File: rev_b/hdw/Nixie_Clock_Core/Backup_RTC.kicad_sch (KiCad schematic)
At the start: 14 parts, among them U1201 DS3231MZ, U1202 TLV6700

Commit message: lots of rev B control board schematic progress
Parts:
- renumbered BT1202 to BT?, BT1201 to BT?, C1202 to C?, C1205 to C?, C1204 to C?, C1203 to C?, C1201 to C?, DOC1201 to DOC?, R1203 to R?, R1201 to R?, R1202 to R?, TP1201 to TP?, U1202 to U?, U1201 to U?

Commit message: more rev b sch progress
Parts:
- removed R?: 1.07M, Resistors_SMD:R_0402, symbol Custom_Library:R_Custom
- added R?: 1M, Resistors_SMD:R_0402, symbol Custom_Library:R_Custom
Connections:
- net VBAT: now also R?.1
- net VBAT_ADC: now also R?.2
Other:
- moved on the sheet: C?, R?, TP?

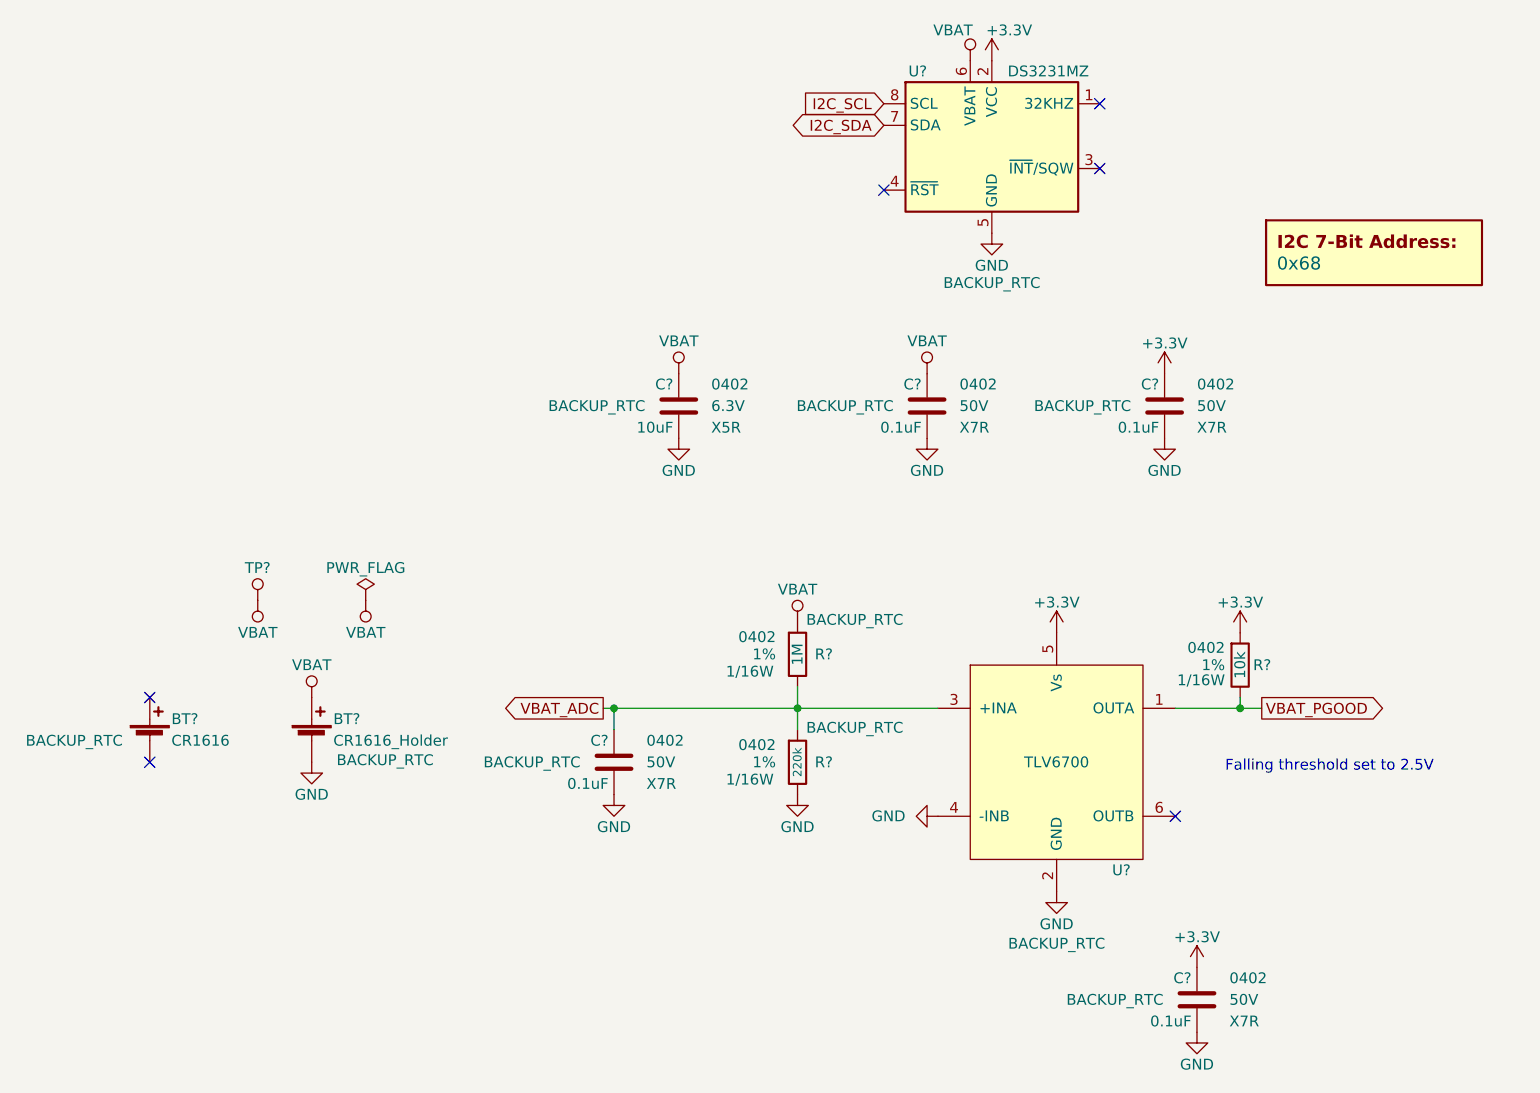
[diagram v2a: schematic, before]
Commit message: updated footprints, ran some DRC
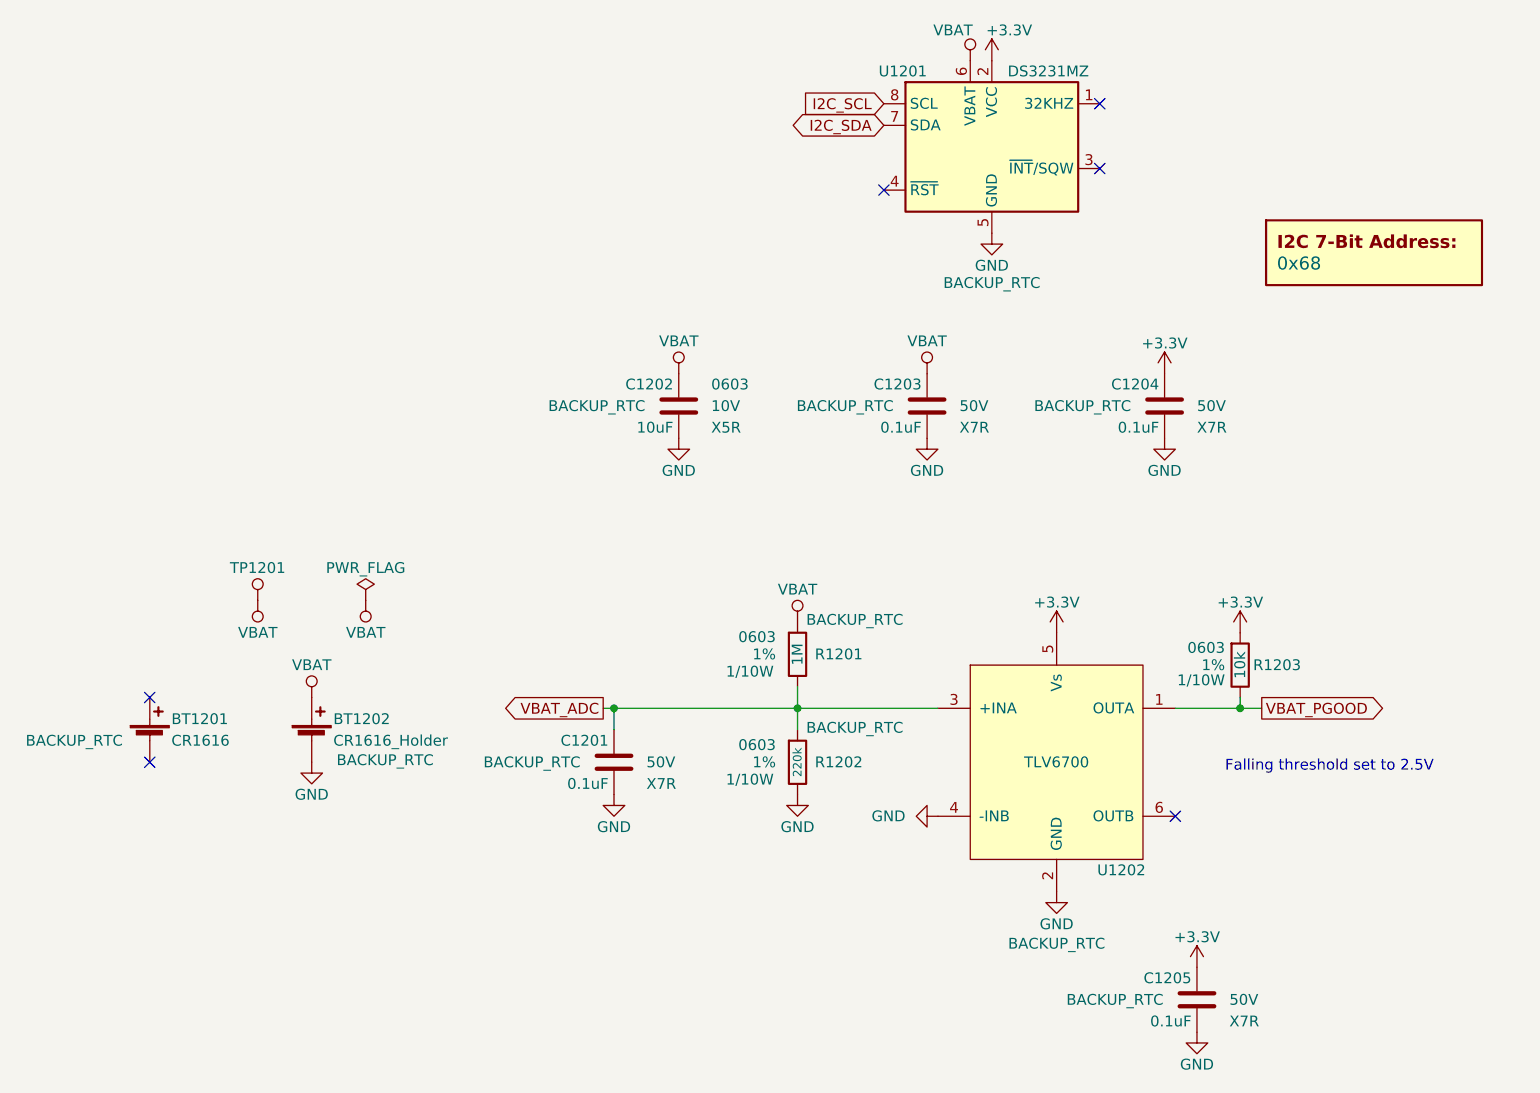
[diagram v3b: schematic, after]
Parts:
- C1201, C1203, C1204, C1205: renamed from C?; footprint Capacitors_SMD:C_0402 -> Capacitors_SMD:C_0603; Digi-Key PN 490-10698-1-ND -> (none); display_footprint 0402 -> (none)
- C1202: renamed from C?; footprint Capacitors_SMD:C_0402 -> Capacitors_SMD:C_0603; Digi-Key PN 1276-1451-1-ND -> (none); Voltage 6.3V -> 10V; display_footprint 0402 -> 0603
- R1201: renamed from R?; footprint Resistors_SMD:R_0402 -> Resistors_SMD:R_0603; Wattage 1/16W -> 1/10W; display_footprint 0402 -> 0603
- R1202: renamed from R?; footprint Resistors_SMD:R_0402 -> Resistors_SMD:R_0603; Digi-Key PN RMCF0402FT220KCT-ND -> (none); Wattage 1/16W -> 1/10W; display_footprint 0402 -> 0603
- R1203: renamed from R?; footprint Resistors_SMD:R_0402 -> Resistors_SMD:R_0603; Digi-Key PN RMCF0402FT10K0CT-ND -> (none); Wattage 1/16W -> 1/10W; display_footprint 0402 -> 0603
- gave numbers to parts that had none: 6

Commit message: hid all passive refdes on core PCB
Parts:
- C1201, C1203, C1204, C1205: Digi-Key PN (none) -> 1276-1935-1-ND; display_footprint (none) -> 0603
- C1202: Digi-Key PN (none) -> 1276-1871-1-ND
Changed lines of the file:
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@@
       (effects (font (size 1.27 1.27)))
     )
-    (property "Digi-Key PN" "" (at 123.19 77.47 0)
+    (property "Digi-Key PN" "1276-1871-1-ND" (at 123.19 77.47 0)
       (effects (font (size 1.27 1.27)) hide)
     )
@@
       (effects (font (size 1.27 1.27)) hide)
     )
-    (property "display_footprint" "" (at 187.96 144.78 0)
+    (property "display_footprint" "0603" (at 187.96 144.78 0)
       (effects (font (size 1.27 1.27)) (justify right))
     )
@@
       (effects (font (size 1.27 1.27)))
     )
-    (property "Digi-Key PN" "" (at 184.15 147.32 0)
+    (property "Digi-Key PN" "1276-1935-1-ND" (at 184.15 147.32 0)
       (effects (font (size 1.27 1.27)) hide)
     )
@@
       (effects (font (size 1.27 1.27)) hide)
     )
-    (property "display_footprint" "" (at 184.15 74.93 0)
+    (property "display_footprint" "0603" (at 184.15 74.93 0)
       (effects (font (size 1.27 1.27)) (justify right))
     )
@@
       (effects (font (size 1.27 1.27)))
     )
-    (property "Digi-Key PN" "" (at 180.34 77.47 0)
+    (property "Digi-Key PN" "1276-1935-1-ND" (at 180.34 77.47 0)
       (effects (font (size 1.27 1.27)) hide)
     )
@@
       (effects (font (size 1.27 1.27)) hide)
     )
-    (property "display_footprint" "" (at 156.21 74.93 0)
+    (property "display_footprint" "0603" (at 156.21 74.93 0)
       (effects (font (size 1.27 1.27)) (justify right))
     )
@@
       (effects (font (size 1.27 1.27)))
     )
-    (property "Digi-Key PN" "" (at 152.4 77.47 0)
+    (property "Digi-Key PN" "1276-1935-1-ND" (at 152.4 77.47 0)
       (effects (font (size 1.27 1.27)) hide)
     )
@@
       (effects (font (size 1.27 1.27)) hide)
     )
-    (property "display_footprint" "" (at 119.38 116.84 0)
+    (property "display_footprint" "0603" (at 119.38 116.84 0)
       (effects (font (size 1.27 1.27)) (justify right))
     )
@@
       (effects (font (size 1.27 1.27)))
     )
-    (property "Digi-Key PN" "" (at 115.57 119.38 0)
-      (effects (font (size 1.27 1.27)) hide)
-    )
+    (property "Digi-Key PN" "1276-1935-1-ND" (at 115.57 119.38 0)
+      (effects (font (size 1.27 1.27)) hide)
+    )

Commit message: added BOM
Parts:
- R1201: Digi-Key PN (none) -> 541-1.00MHCT-ND
- R1202: Digi-Key PN (none) -> 541-4039-1-ND
- R1203: Digi-Key PN (none) -> 541-10.0KHCT-ND
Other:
- title: (none) -> Nixie Clock Redux Core Board
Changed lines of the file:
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@@
   (paper "A")
   (title_block
-    (date "2023-05-12")
-    (rev "PRELIM")
+    (title "Nixie Clock Redux Core Board")
+    (date "2023-07-30")
+    (rev "B")
     (company "Drew Maatman")
   )
@@
     (effects (font (size 1.27 1.27)) (justify left bottom))
   )
-  (global_label "VBAT_ADC" (shape output) (at 114.3 113.03 180)
+  (global_label "VBAT_ADC" (shape output) (at 114.3 113.03 180) (fields_autoplaced)
     (effects (font (size 1.27 1.27)) (justify right))
-    (property "Intersheetrefs" "${INTERSHEET_REFS}" (at 114.3 113.03 0)
-      (effects (font (size 1.27 1.27)) hide)
-    )
-  )
-  (global_label "I2C_SDA" (shape bidirectional) (at 147.32 44.45 180)
+    (property "Intersheetrefs" "${INTERSHEET_REFS}" (at 102.3832 113.03 0)
+      (effects (font (size 1.27 1.27)) (justify right))
+    )
+  )
+  (global_label "I2C_SDA" (shape bidirectional) (at 147.32 44.45 180) (fields_autoplaced)
     (effects (font (size 1.27 1.27)) (justify right))
-    (property "Intersheetrefs" "${INTERSHEET_REFS}" (at 147.32 44.45 0)
-      (effects (font (size 1.27 1.27)) hide)
-    )
-  )
-  (global_label "I2C_SCL" (shape input) (at 147.32 41.91 180)
+    (property "Intersheetrefs" "${INTERSHEET_REFS}" (at 135.6829 44.45 0)
+      (effects (font (size 1.27 1.27)) (justify right))
+    )
+  )
+  (global_label "I2C_SCL" (shape input) (at 147.32 41.91 180) (fields_autoplaced)
     (effects (font (size 1.27 1.27)) (justify right))
-    (property "Intersheetrefs" "${INTERSHEET_REFS}" (at 147.32 41.91 0)
-      (effects (font (size 1.27 1.27)) hide)
-    )
-  )
-  (global_label "VBAT_PGOOD" (shape output) (at 191.77 113.03 0)
+    (property "Intersheetrefs" "${INTERSHEET_REFS}" (at 136.8547 41.91 0)
+      (effects (font (size 1.27 1.27)) (justify right))
+    )
+  )
+  (global_label "VBAT_PGOOD" (shape output) (at 191.77 113.03 0) (fields_autoplaced)
     (effects (font (size 1.27 1.27)) (justify left))
-    (property "Intersheetrefs" "${INTERSHEET_REFS}" (at 191.77 113.03 0)
-      (effects (font (size 1.27 1.27)) hide)
+    (property "Intersheetrefs" "${INTERSHEET_REFS}" (at 206.5292 113.03 0)
+      (effects (font (size 1.27 1.27)) (justify left))
     )
   )
@@
       (effects (font (size 1.27 1.27)) (justify left))
     )
-    (property "Digi-Key PN" "" (at 189.23 107.95 0)
+    (property "Digi-Key PN" "541-10.0KHCT-ND" (at 189.23 107.95 0)
       (effects (font (size 1.27 1.27)) hide)
     )
@@
       (effects (font (size 1.27 1.27)) (justify right))
     )
-    (property "Digi-Key PN" "" (at 137.16 119.38 0)
+    (property "Digi-Key PN" "541-4039-1-ND" (at 137.16 119.38 0)
       (effects (font (size 1.27 1.27)) hide)
     )
@@
       (effects (font (size 1.27 1.27)) (justify right))
     )
-    (property "Digi-Key PN" "" (at 137.16 106.68 0)
-      (effects (font (size 1.27 1.27)) hide)
-    )
+    (property "Digi-Key PN" "541-1.00MHCT-ND" (at 137.16 106.68 0)
+      (effects (font (size 1.27 1.27)) hide)
+    )
